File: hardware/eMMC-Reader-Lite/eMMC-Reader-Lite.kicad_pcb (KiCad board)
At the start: 2 copper layers, 39.4 x 25.4 mm, 36 parts, among them J1 Conn_01x09_Socket, J2 USB_B_Mini, U2 TXS02612, U3 W25X20CLSN, U4 LM1117MP-1.8

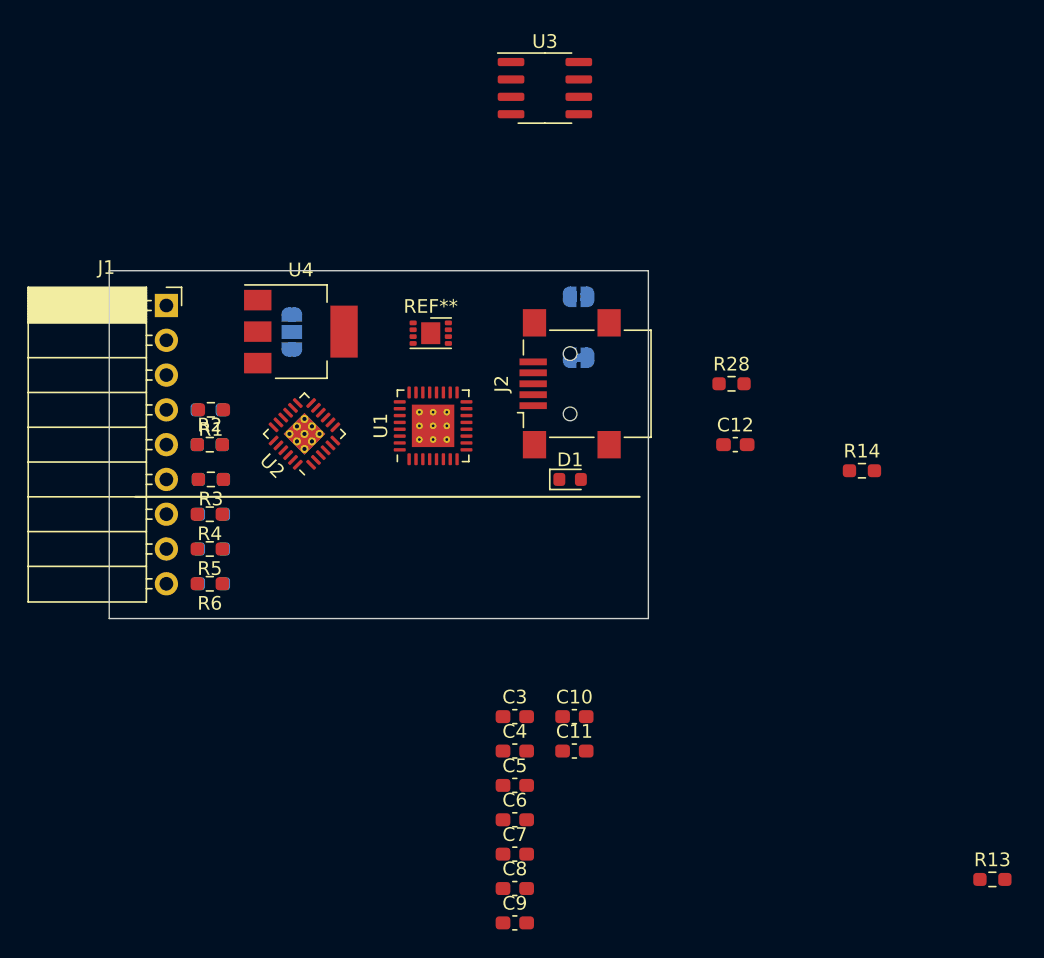
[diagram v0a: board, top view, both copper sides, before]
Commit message: Further routing
Need fills, GL3224 test points, length-matching from GL3224

Might need more blinky
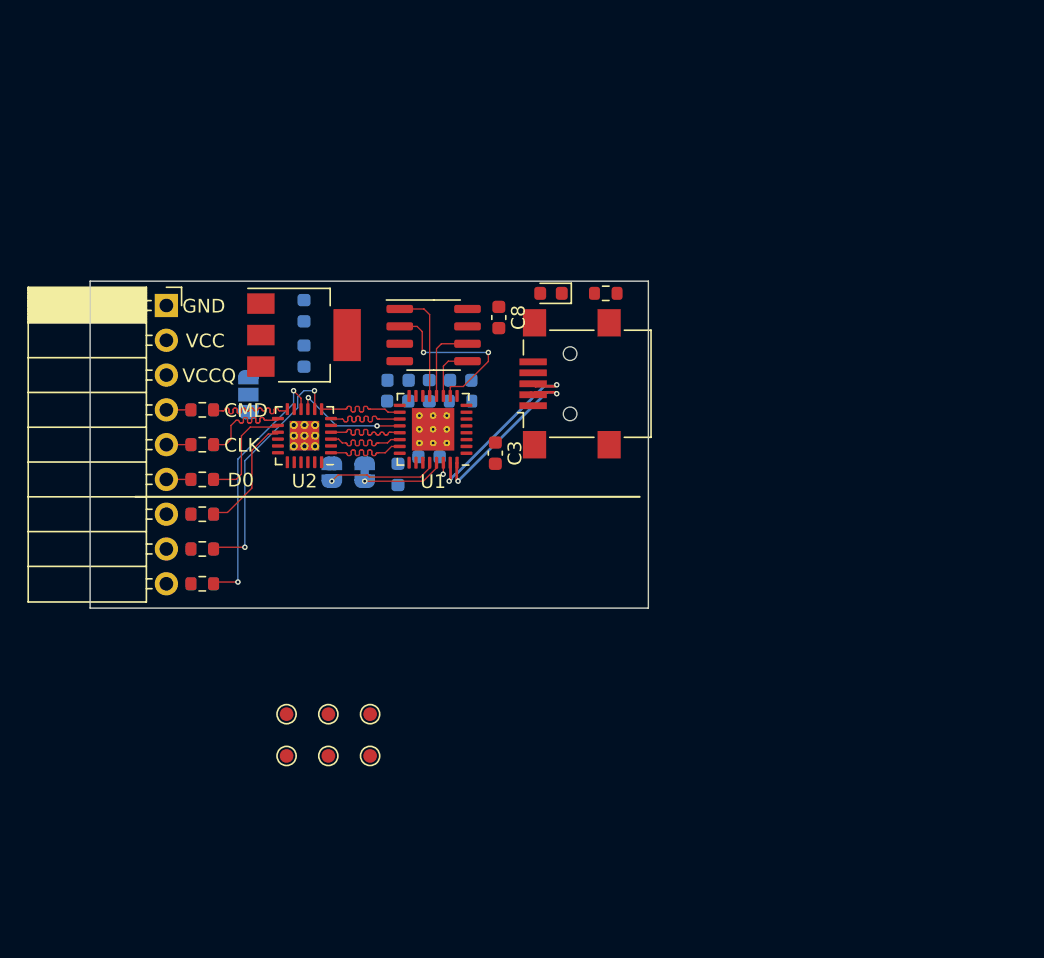
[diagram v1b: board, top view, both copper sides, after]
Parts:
- removed C12: 0.1uF, Capacitor_SMD:C_0603_1608Metric_Pad1.08x0.95mm_HandSolder
- removed R28: 330, Resistor_SMD:R_0603_1608Metric_Pad0.98x0.95mm_HandSolder
- removed REF**: SON-8-1EP_3x2mm_P0.5mm_EP1.4x1.6mm, Package_SON:SON-8-1EP_3x2mm_P0.5mm_EP1.4x1.6mm
- added C1: 0.1uF, Capacitor_SMD:C_0603_1608Metric, B.Cu at (141.7, 73.9)
- added TP1: TestPoint_Small, TestPoint:TestPoint_Pad_D1.0mm, F.Cu at (133.6, 91.4)
- added TP2: TestPoint_Small, TestPoint:TestPoint_Pad_D1.0mm, F.Cu at (133.6, 94.5)
- added TP3: TestPoint_Small, TestPoint:TestPoint_Pad_D1.0mm, F.Cu at (136.7, 91.4)
- added TP4: TestPoint_Small, TestPoint:TestPoint_Pad_D1.0mm, F.Cu at (136.7, 94.5)
- added TP5: TestPoint_Small, TestPoint:TestPoint_Pad_D1.0mm, F.Cu at (139.7, 91.4)
- added TP6: TestPoint_Small, TestPoint:TestPoint_Pad_D1.0mm, F.Cu at (139.7, 94.5)
- C10, C11, C4, C5, C6, C7, C9: footprint Capacitor_SMD:C_0603_1608Metric_Pad1.08x0.95mm_HandSolder -> Capacitor_SMD:C_0603_1608Metric; moved to B.Cu
- C3, C8: footprint Capacitor_SMD:C_0603_1608Metric_Pad1.08x0.95mm_HandSolder -> Capacitor_SMD:C_0603_1608Metric
- R1, R10, R11, R12, R13, R2, R3, R4, R5, R6, R7, R8, R9: footprint Resistor_SMD:R_0603_1608Metric_Pad0.98x0.95mm_HandSolder -> Resistor_SMD:R_0603_1608Metric
- R14: footprint Resistor_SMD:R_0603_1608Metric_Pad0.98x0.95mm_HandSolder -> Resistor_SMD:R_0603_1608Metric; moved to B.Cu
- moved R13 51.3 mm to (156.9, 60.7)
- moved C8 41.7 mm to (149.1, 62.5), turned to -90 degrees
- moved C9 39.4 mm to (144.0, 67.8), turned to -90 degrees
- moved C11 37.7 mm to (134.9, 62.0), turned to 90 degrees
- moved C6 33.2 mm to (141.7, 67.1), turned to 180 degrees
- moved C10 32.9 mm to (134.9, 65.3), turned to 90 degrees
- moved C5 29.8 mm to (146.3, 67.1), turned to 180 degrees
- moved R14 29.8 mm to (146.3, 68.6), turned to 180 degrees
- moved C7 29.7 mm to (144.0, 72.6)
- moved C4 26.9 mm to (141.7, 68.6)
- moved JP1 22.1 mm to (136.9, 73.8), turned to 90 degrees
- moved U3 19.8 mm to (144.3, 63.8)
- moved C3 19.3 mm to (148.8, 72.4), turned to -90 degrees
- moved JP2 17.7 mm to (139.3, 73.8), turned to 90 degrees
- moved D1 13.7 mm to (152.9, 60.7), turned to 180 degrees
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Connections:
- net Net-(J2-D+) renamed /D+
- net Net-(J2-D-) renamed /D-
- C6 pad 1: Net-(C6-Pad1) -> +3V3
- C7 pad 1: Net-(C7-Pad1) -> +3V3
- J2 pad 6: Net-(J2-Shield) -> GND
- R1 pad 1: Net-(U2-CMDB_0) -> Net-(U2-CMDB_1)
- R2 pad 1: Net-(U2-CLKB_0) -> Net-(U2-CLKB_1)
- R3 pad 1: Net-(U2-DAT0B_0) -> Net-(U2-DAT0B_1)
- R4 pad 1: Net-(U2-DAT1B_0) -> Net-(U2-DAT1B_1)
- R5 pad 1: Net-(U2-DAT2B_0) -> Net-(U2-DAT2B_1)
- R6 pad 1: Net-(U2-DAT3B_0) -> Net-(U2-DAT3B_1)
- U1 pad 16: Net-(C6-Pad1) -> +3V3
- U1 pad 24: Net-(U1A-SD_VCCQ) -> /VCCA
- U1 pad 25: Net-(C7-Pad1) -> +3V3
- U1 pad 27: (no net) -> GND
- U2 pad 10: unconnected-(U2-DAT3B_1-Pad10) -> Net-(U2-DAT3B_1)
- U2 pad 12: unconnected-(U2-CMDB_1-Pad12) -> Net-(U2-CMDB_1)
- U2 pad 13: unconnected-(U2-CLKB_1-Pad13) -> Net-(U2-CLKB_1)
- U2 pad 14: unconnected-(U2-DAT0B_1-Pad14) -> Net-(U2-DAT0B_1)
- U2 pad 15: unconnected-(U2-DAT1B_1-Pad15) -> Net-(U2-DAT1B_1)
- U2 pad 16: Net-(U2-DAT1B_0) -> unconnected-(U2-DAT1B_0-Pad16)
- U2 pad 17: unconnected-(U2-VCCB_1-Pad17) -> VCCQ
- U2 pad 18: Net-(U2-DAT0B_0) -> unconnected-(U2-DAT0B_0-Pad18)
- U2 pad 19: Net-(U2-CLKB_0) -> unconnected-(U2-CLKB_0-Pad19)
- U2 pad 20: Net-(U2-CMDB_0) -> unconnected-(U2-CMDB_0-Pad20)
- U2 pad 21: VCCQ -> unconnected-(U2-VCCB_0-Pad21)
- U2 pad 22: Net-(U2-DAT3B_0) -> unconnected-(U2-DAT3B_0-Pad22)
- U2 pad 23: Net-(U2-DAT2B_0) -> unconnected-(U2-DAT2B_0-Pad23)
- U2 pad 24: GND -> /VCCA
- U2 pad 5: Net-(U1A-SD_VCCQ) -> /VCCA
- U2 pad 8: unconnected-(U2-DAT2B_1-Pad8) -> Net-(U2-DAT2B_1)
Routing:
- net Net-(U2-DAT3B_1): track 0.00 -> 19.1 mm, vias 0 -> 2
- net Net-(U2-DAT2B_1): track 0.00 -> 17.8 mm, vias 0 -> 2
- net /D+: track 0.00 -> 14.0 mm, vias 0 -> 2
- net /D-: track 0.00 -> 13.4 mm, vias 0 -> 2
- net Net-(U1B-SPI_MISO): track 0.00 -> 13.0 mm, vias 0 -> 2
- net Net-(U2-DAT1B_1): track 0.00 -> 8.74 mm
- net Net-(U1A-SD_CLK): track 0.00 -> 8.42 mm, vias 0 -> 2
- net Net-(U1B-SPI_CS): track 0.00 -> 8.30 mm
- net Net-(U2-CMDB_1): track 0.00 -> 8.15 mm
- net /SD_WP: track 0.00 -> 8.05 mm, vias 0 -> 1
- net Net-(U2-DAT0B_1): track 0.00 -> 7.92 mm
- net Net-(U2-CLKB_1): track 0.00 -> 7.77 mm
- net Net-(U1A-SD_D0): track 0.00 -> 7.29 mm
- net Net-(U1A-SD_D3): track 0.00 -> 7.28 mm
- net Net-(U1A-SD_D2): track 0.00 -> 7.26 mm
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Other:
- board size 39.4 x 25.4 mm -> 40.8 x 23.9 mm
- board text added: "1V8"
- board text added: "3V3"
- board text added: "CLK"
- board text added: "CMD"
- board text added: "Card Present"
- board text added: "D1"
- board text added: "D2"
- board text added: "D3"
- board text added: "GL3224 + TXS02612"
- board text added: "GND"
- board text added: "Signal Logic Level"
- board text added: "VCC"
- board text added: "VCCQ"
- board text added: "Write Protect"
- board text added: "eMMC Friend"

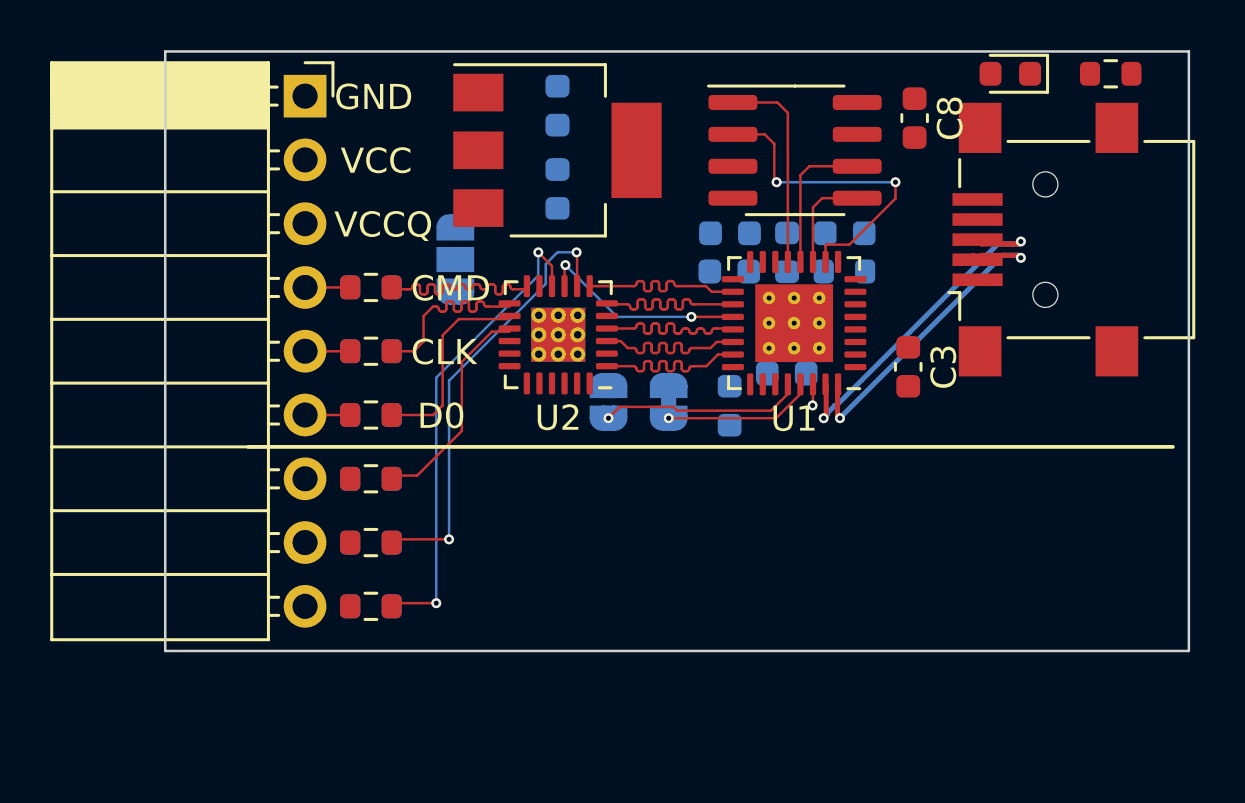
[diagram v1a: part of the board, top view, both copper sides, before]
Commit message: Break out SD_VCC output rail to be distinct from 3V3 net
Add indicator LED for that rail
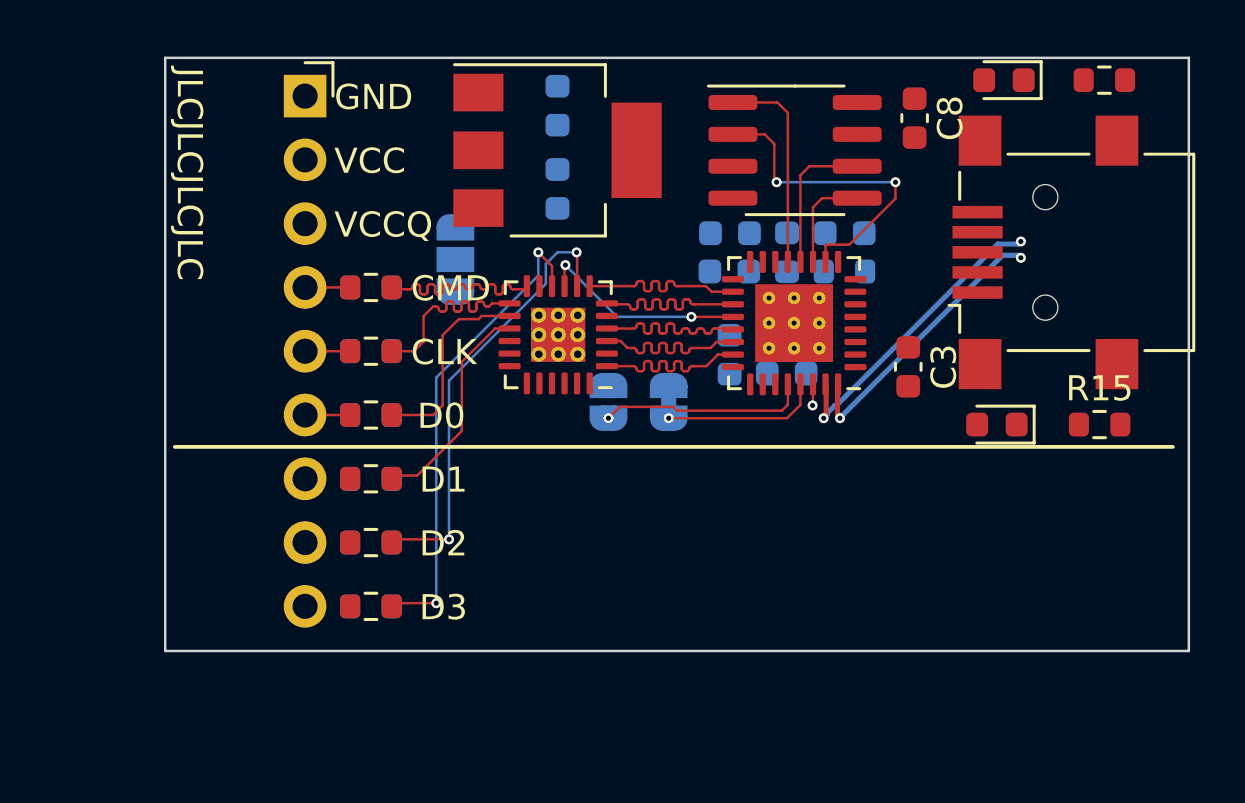
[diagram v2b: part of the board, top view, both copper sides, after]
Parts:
- added D2: LED_Small_Filled, LED_SMD:LED_0603_1608Metric, F.Cu at (152.4, 74.7)
- added R15: 220, Resistor_SMD:R_0603_1608Metric, F.Cu at (156.5, 74.7)
- moved C1 2.03 mm to (141.7, 71.9), turned to 90 degrees
- moved J2 0.51 mm to (154.3, 67.8)
- moved D1 0.36 mm to (152.7, 61.0)
- moved R13 0.36 mm to (156.7, 61.0)
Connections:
- C10 pad 1: +3V3 -> /SD_VCC
- J1 pad 2: +3V3 -> /SD_VCC
- JP3 pad 3: +3V3 -> /SD_VCC
- U1 pad 26: +3V3 -> /SD_VCC
- U4 pad 3: +3V3 -> /SD_VCC
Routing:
- net /D-: track 13.4 -> 11.3 mm
- net /D+: track 14.0 -> 12.2 mm
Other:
- board size 40.8 x 23.9 mm -> 40.8 x 23.6 mm
- board text added: "JLCJLCJLCJLC"
- board text added: "by squidgeefish"
